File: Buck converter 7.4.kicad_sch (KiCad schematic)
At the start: 41 parts

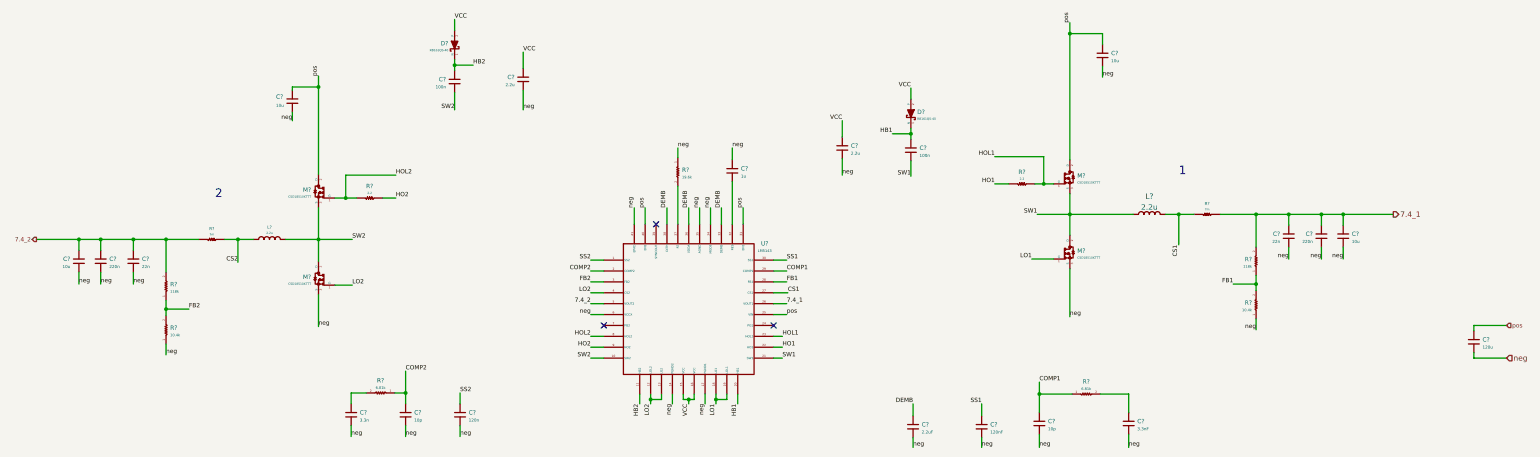
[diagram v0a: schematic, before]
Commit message: reference designator added
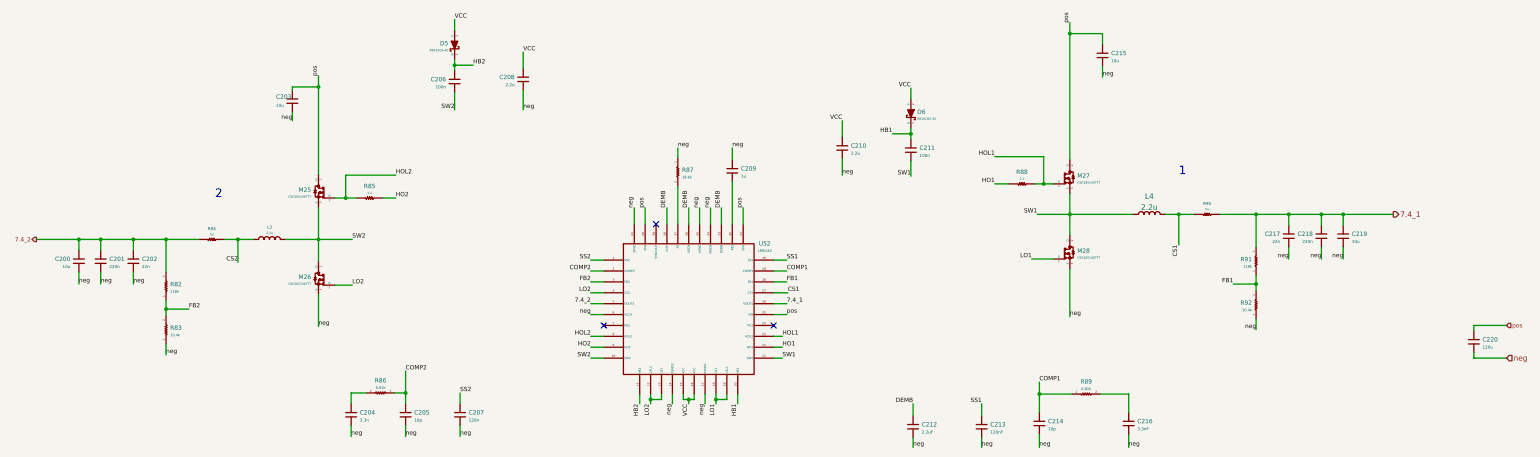
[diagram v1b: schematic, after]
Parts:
- gave numbers to parts that had none: 41

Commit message: changing some capacitors
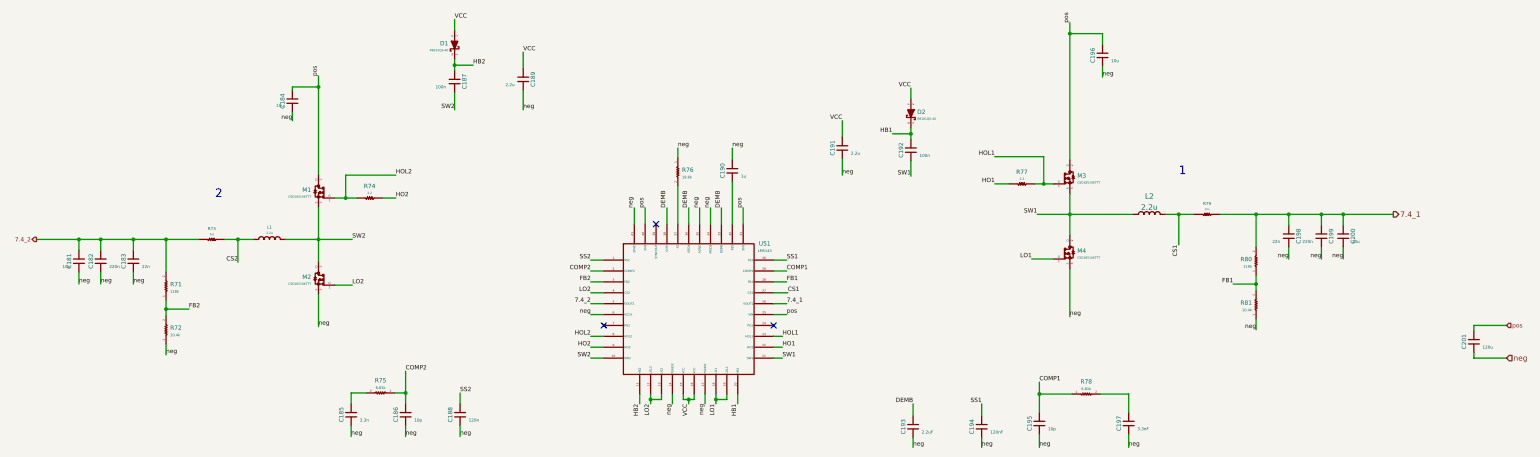
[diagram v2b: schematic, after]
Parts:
- C181: renamed from C200; symbol Capacitors:C0603X105J4RACTU -> Capacitors:C0603xxxxxxxxxxx
- C182: renamed from C201; symbol Capacitors:C0603X105J4RACTU -> Capacitors:C0603xxxxxxxxxxx
- C183: renamed from C202; symbol Capacitors:C0603X105J4RACTU -> Capacitors:C0603xxxxxxxxxxx
- C184: renamed from C203; symbol Capacitors:C0603X105J4RACTU -> Capacitors:C0603xxxxxxxxxxx
- C185: renamed from C204; symbol Capacitors:C0603X105J4RACTU -> Capacitors:C0603xxxxxxxxxxx
- C186: renamed from C205; symbol Capacitors:C0603X105J4RACTU -> Capacitors:C0603xxxxxxxxxxx
- C187: renamed from C206; symbol Capacitors:C0603X105J4RACTU -> Capacitors:C0603xxxxxxxxxxx
- C188: renamed from C207; symbol Capacitors:C0603X105J4RACTU -> Capacitors:C0603xxxxxxxxxxx
- C189: renamed from C208; symbol Capacitors:C0603X105J4RACTU -> Capacitors:C0603xxxxxxxxxxx
- C190: renamed from C209; symbol Capacitors:C0603X105J4RACTU -> Capacitors:C0603xxxxxxxxxxx
- C191: renamed from C210; symbol Capacitors:C0603X105J4RACTU -> Capacitors:C0603xxxxxxxxxxx
- C192: renamed from C211; symbol Capacitors:C0603X105J4RACTU -> Capacitors:C0603xxxxxxxxxxx
- C193: renamed from C212; symbol Capacitors:C0603X105J4RACTU -> Capacitors:C0603xxxxxxxxxxx
- C194: renamed from C213; symbol Capacitors:C0603X105J4RACTU -> Capacitors:C0603xxxxxxxxxxx
- C195: renamed from C214; symbol Capacitors:C0603X105J4RACTU -> Capacitors:C0603xxxxxxxxxxx
- C196: renamed from C215; symbol Capacitors:C0603X105J4RACTU -> Capacitors:C0603xxxxxxxxxxx
- C197: renamed from C216; symbol Capacitors:C0603X105J4RACTU -> Capacitors:C0603xxxxxxxxxxx
- C198: renamed from C217; symbol Capacitors:C0603X105J4RACTU -> Capacitors:C0603xxxxxxxxxxx
- C199: renamed from C218; symbol Capacitors:C0603X105J4RACTU -> Capacitors:C0603xxxxxxxxxxx
- C200: renamed from C219; symbol Capacitors:C0603X105J4RACTU -> Capacitors:C0603xxxxxxxxxxx
- C201: renamed from C220; symbol Capacitors:C0603X105J4RACTU -> Capacitors:C0603xxxxxxxxxxx
- renumbered D5 to D1, D6 to D2, L3 to L1, L4 to L2, M25 to M1, M26 to M2, M27 to M3, M28 to M4, R82 to R71, R83 to R72, R84 to R73, R85 to R74, R86 to R75, R87 to R76, R88 to R77, R89 to R78, R90 to R79, R91 to R80, R92 to R81, U52 to U51

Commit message: base schematic and PCB made
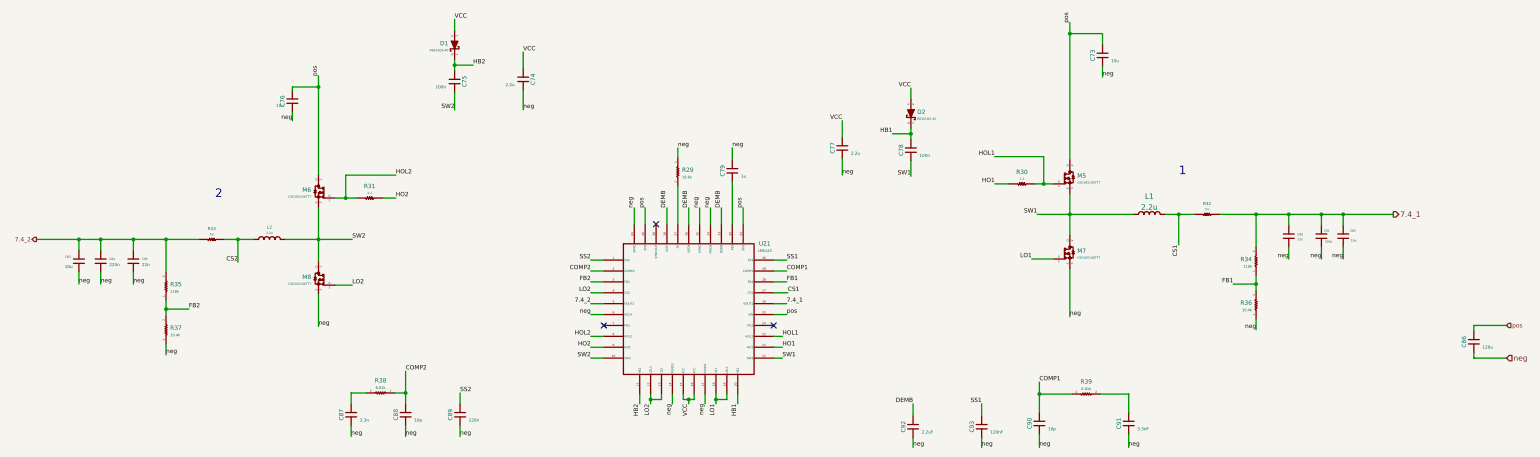
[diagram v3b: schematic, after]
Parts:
- C73: renamed from C196; footprint my_footprints:C0603X105J4RACTU -> Capacitors:C0603X105J4RACTU
- C74: renamed from C189; footprint my_footprints:C0603X105J4RACTU -> Capacitors:C0603X105J4RACTU
- C75: renamed from C187; footprint my_footprints:C0603X105J4RACTU -> Capacitors:C0603X105J4RACTU
- C76: renamed from C184; footprint my_footprints:C0603X105J4RACTU -> Capacitors:C0603X105J4RACTU
- C77: renamed from C191; footprint my_footprints:C0603X105J4RACTU -> Capacitors:C0603X105J4RACTU
- C78: renamed from C192; footprint my_footprints:C0603X105J4RACTU -> Capacitors:C0603X105J4RACTU
- C79: renamed from C190; footprint my_footprints:C0603X105J4RACTU -> Capacitors:C0603X105J4RACTU
- C80: renamed from C198; footprint my_footprints:C0603X105J4RACTU -> Capacitors:C0603X105J4RACTU
- C81: renamed from C199; footprint my_footprints:C0603X105J4RACTU -> Capacitors:C0603X105J4RACTU
- C82: renamed from C200; footprint my_footprints:C0603X105J4RACTU -> Capacitors:C0603X105J4RACTU
- C83: renamed from C181; footprint my_footprints:C0603X105J4RACTU -> Capacitors:C0603X105J4RACTU
- C84: renamed from C182; footprint my_footprints:C0603X105J4RACTU -> Capacitors:C0603X105J4RACTU
- C85: renamed from C183; footprint my_footprints:C0603X105J4RACTU -> Capacitors:C0603X105J4RACTU
- C86: renamed from C201; footprint my_footprints:C0603X105J4RACTU -> Capacitors:C0603X105J4RACTU
- C87: renamed from C185; footprint my_footprints:C0603X105J4RACTU -> Capacitors:C0603X105J4RACTU
- C88: renamed from C186; footprint my_footprints:C0603X105J4RACTU -> Capacitors:C0603X105J4RACTU
- C89: renamed from C188; footprint my_footprints:C0603X105J4RACTU -> Capacitors:C0603X105J4RACTU
- C90: renamed from C195; footprint my_footprints:C0603X105J4RACTU -> Capacitors:C0603X105J4RACTU
- C91: renamed from C197; footprint my_footprints:C0603X105J4RACTU -> Capacitors:C0603X105J4RACTU
- C92: renamed from C193; footprint my_footprints:C0603X105J4RACTU -> Capacitors:C0603X105J4RACTU
- C93: renamed from C194; footprint my_footprints:C0603X105J4RACTU -> Capacitors:C0603X105J4RACTU
- D1, D2: footprint my_footprints:RB161QS-40T18R -> Diodes:RB161QS-40T18R; symbol diodes:RB161QS-40 -> Diodes:RB161QS-40
- L1: renamed from L2; footprint (none) -> Inductors:SBC9-2R2-792
- L2: renamed from L1; footprint (none) -> Inductors:SBC9-2R2-792
- M5: renamed from M3; footprint my_footprints:CSD18510KTTT -> E-MOSFETs:CSD18510KTTT
- M6: renamed from M1; footprint my_footprints:CSD18510KTTT -> E-MOSFETs:CSD18510KTTT
- M7: renamed from M4; footprint my_footprints:CSD18510KTTT -> E-MOSFETs:CSD18510KTTT
- M8: renamed from M2; footprint my_footprints:CSD18510KTTT -> E-MOSFETs:CSD18510KTTT
- R29: renamed from R76; footprint my_footprints:MCR03EZPFX -> Resistors:MCR03EZPFX; symbol resistors:MCR03EZPFX -> Resistors:MCR03EZPFX
- R30: renamed from R77; footprint my_footprints:MCR03EZPFL -> Resistors:MCR03EZPFL; symbol resistors:MCR03EZPFL -> Resistors:MCR03EZPFL
- R31: renamed from R74; footprint my_footprints:MCR03EZPFL -> Resistors:MCR03EZPFL; symbol resistors:MCR03EZPFL -> Resistors:MCR03EZPFL
- R32: renamed from R79; footprint my_footprints:UCR18EVH -> Resistors:UCR18EVH; symbol resistors:UCR18EVH -> Resistors:UCR18EVH
- R33: renamed from R73; footprint my_footprints:UCR18EVH -> Resistors:UCR18EVH; symbol resistors:UCR18EVH -> Resistors:UCR18EVH
- R34: renamed from R80; footprint my_footprints:MCR03EZPFX -> Resistors:MCR03EZPFX; symbol resistors:MCR03EZPFX -> Resistors:MCR03EZPFX
- R35: renamed from R71; footprint my_footprints:MCR03EZPFX -> Resistors:MCR03EZPFX; symbol resistors:MCR03EZPFX -> Resistors:MCR03EZPFX
- R36: renamed from R81; footprint my_footprints:MCR03EZPFX -> Resistors:MCR03EZPFX; symbol resistors:MCR03EZPFX -> Resistors:MCR03EZPFX
- R37: renamed from R72; footprint my_footprints:MCR03EZPFX -> Resistors:MCR03EZPFX; symbol resistors:MCR03EZPFX -> Resistors:MCR03EZPFX
- R38: renamed from R75; footprint my_footprints:MCR03EZPFX -> Resistors:MCR03EZPFX; symbol resistors:MCR03EZPFX -> Resistors:MCR03EZPFX
- R39: renamed from R78; footprint my_footprints:MCR03EZPFX -> Resistors:MCR03EZPFX; symbol resistors:MCR03EZPFX -> Resistors:MCR03EZPFX
- U21: renamed from U51; footprint my_footprints:LM5143RHAR -> ICs:LM5143RHAR

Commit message: minor changes
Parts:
- C73, C76, C82, C83: value 10u -> (none); footprint Capacitors:C0603X105J4RACTU -> (none)
- C74, C77: value 2.2u -> (none); footprint Capacitors:C0603X105J4RACTU -> (none)
- C75, C78: value 100n -> (none); footprint Capacitors:C0603X105J4RACTU -> (none)
- C79: value 1u -> (none); footprint Capacitors:C0603X105J4RACTU -> (none)
- C80, C85: value 22n -> (none); footprint Capacitors:C0603X105J4RACTU -> (none)
- C81, C84: value 220n -> (none); footprint Capacitors:C0603X105J4RACTU -> (none)
- C86: value 120u -> (none); footprint Capacitors:C0603X105J4RACTU -> (none)
- C87: value 3.3n -> (none); footprint Capacitors:C0603X105J4RACTU -> (none)
- C88, C90: value 10p -> (none); footprint Capacitors:C0603X105J4RACTU -> (none)
- C89: value 120n -> (none); footprint Capacitors:C0603X105J4RACTU -> (none)
- C91: value 3.3nF -> (none); footprint Capacitors:C0603X105J4RACTU -> (none)
- C92: value 2.2uF -> (none); footprint Capacitors:C0603X105J4RACTU -> (none)
- C93: value 120nF -> (none); footprint Capacitors:C0603X105J4RACTU -> (none)
- D1, D2: value RB161QS-40 -> (none); footprint Diodes:RB161QS-40T18R -> (none)
- L1, L2: value 2.2u -> (none); footprint Inductors:SBC9-2R2-792 -> (none)
- M5, M6, M7, M8: value CSD18510KTTT -> (none); footprint E-MOSFETs:CSD18510KTTT -> (none)
- R29: value 19.6k -> (none); footprint Resistors:MCR03EZPFX -> (none)
- R30, R31: value 2.2 -> (none); footprint Resistors:MCR03EZPFL -> (none)
- R32, R33: value 7m -> (none); footprint Resistors:UCR18EVH -> (none)
- R34, R35: value 118k -> (none); footprint Resistors:MCR03EZPFX -> (none)
- R36, R37: value 10.4k -> (none); footprint Resistors:MCR03EZPFX -> (none)
- R38, R39: value 6.81k -> (none); footprint Resistors:MCR03EZPFX -> (none)
- U21: value LM5143 -> (none); footprint ICs:LM5143RHAR -> (none)
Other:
- company: (none) -> 3D ROBOT
- title: 3D robot project - electronics -> Base circuit - TH

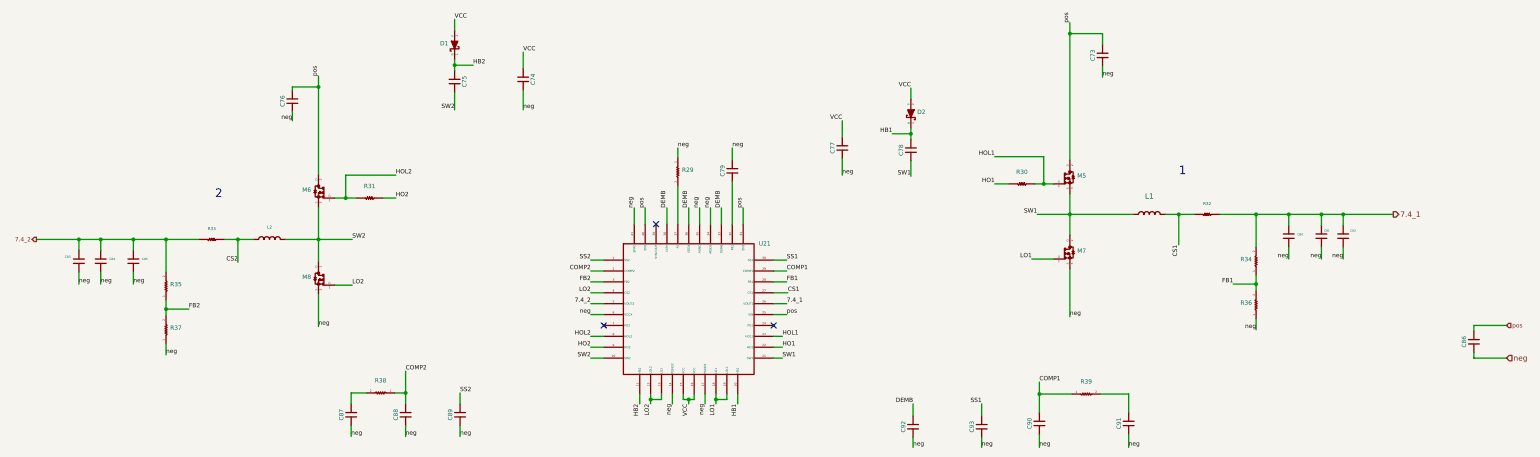
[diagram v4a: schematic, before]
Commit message: make a TH version of the base PCB for testing purposes...
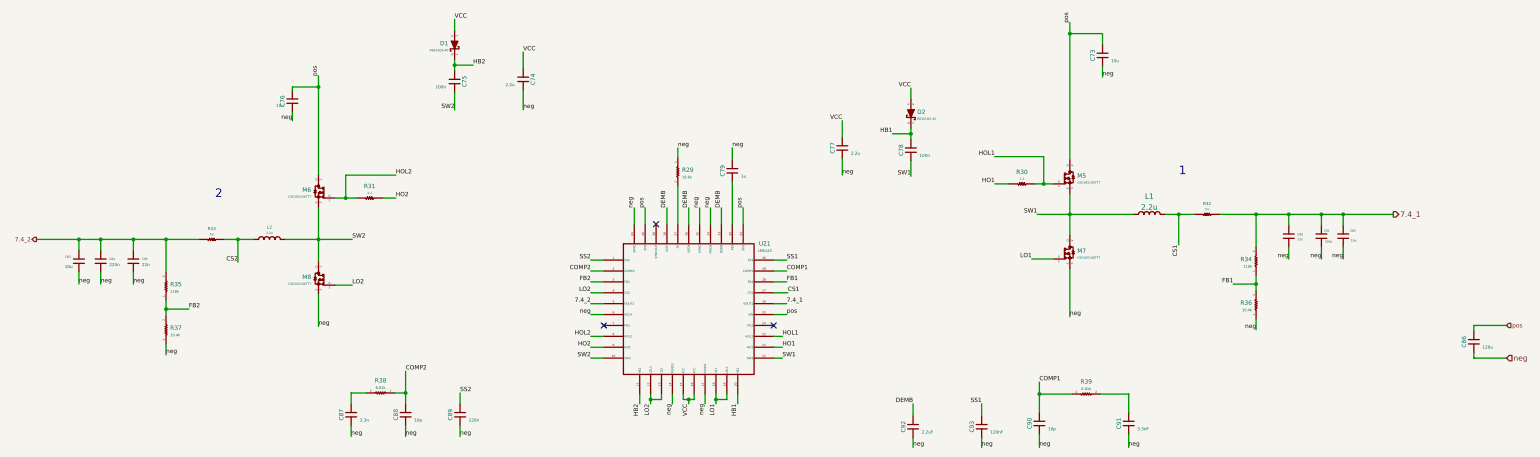
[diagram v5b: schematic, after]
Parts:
- C73, C76, C82, C83: value (none) -> 10u; footprint (none) -> Capacitors:C0603X105J4RACTU
- C74, C77: value (none) -> 2.2u; footprint (none) -> Capacitors:C0603X105J4RACTU
- C75, C78: value (none) -> 100n; footprint (none) -> Capacitors:C0603X105J4RACTU
- C79: value (none) -> 1u; footprint (none) -> Capacitors:C0603X105J4RACTU
- C80, C85: value (none) -> 22n; footprint (none) -> Capacitors:C0603X105J4RACTU
- C81, C84: value (none) -> 220n; footprint (none) -> Capacitors:C0603X105J4RACTU
- C86: value (none) -> 120u; footprint (none) -> Capacitors:C0603X105J4RACTU
- C87: value (none) -> 3.3n; footprint (none) -> Capacitors:C0603X105J4RACTU
- C88, C90: value (none) -> 10p; footprint (none) -> Capacitors:C0603X105J4RACTU
- C89: value (none) -> 120n; footprint (none) -> Capacitors:C0603X105J4RACTU
- C91: value (none) -> 3.3nF; footprint (none) -> Capacitors:C0603X105J4RACTU
- C92: value (none) -> 2.2uF; footprint (none) -> Capacitors:C0603X105J4RACTU
- C93: value (none) -> 120nF; footprint (none) -> Capacitors:C0603X105J4RACTU
- D1, D2: value (none) -> RB161QS-40; footprint (none) -> Diodes:RB161QS-40T18R
- L1, L2: value (none) -> 2.2u; footprint (none) -> Inductors:SBC9-2R2-792
- M5, M6, M7, M8: value (none) -> CSD18510KTTT; footprint (none) -> E-MOSFETs:CSD18510KTTT
- R29: value (none) -> 19.6k; footprint (none) -> Resistors:MCR03EZPFX
- R30, R31: value (none) -> 2.2; footprint (none) -> Resistors:MCR03EZPFL
- R32, R33: value (none) -> 7m; footprint (none) -> Resistors:UCR18EVH
- R34, R35: value (none) -> 118k; footprint (none) -> Resistors:MCR03EZPFX
- R36, R37: value (none) -> 10.4k; footprint (none) -> Resistors:MCR03EZPFX
- R38, R39: value (none) -> 6.81k; footprint (none) -> Resistors:MCR03EZPFX
- U21: value (none) -> LM5143; footprint (none) -> ICs:LM5143RHAR
